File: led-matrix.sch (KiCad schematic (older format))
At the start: 32 parts

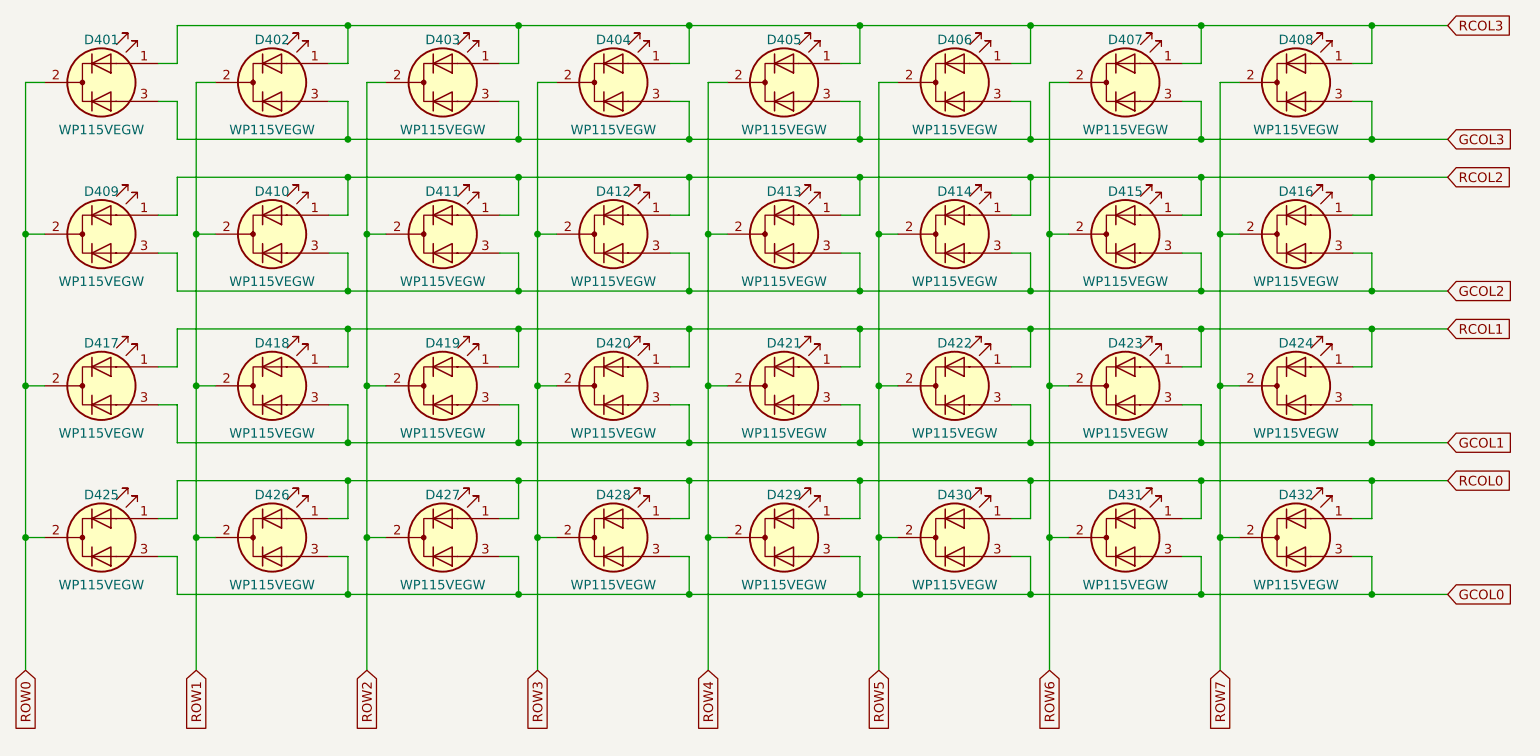
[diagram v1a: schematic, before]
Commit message: renamed led references D -> LED
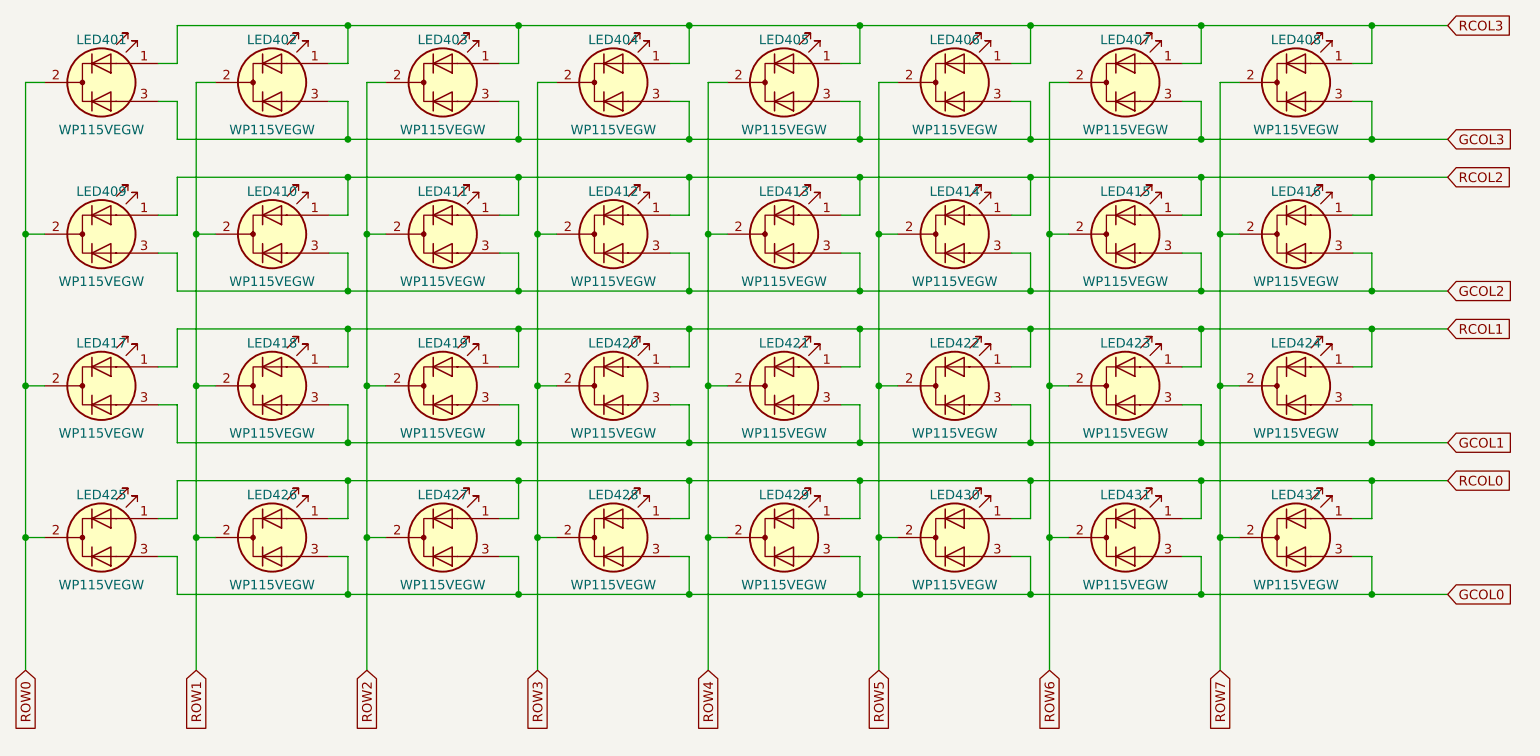
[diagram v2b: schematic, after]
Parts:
- renumbered D401 to LED401, D402 to LED402, D403 to LED403, D404 to LED404, D405 to LED405, D406 to LED406, D407 to LED407, D408 to LED408, D409 to LED409, D410 to LED410, D411 to LED411, D412 to LED412, D413 to LED413, D414 to LED414, D415 to LED415, D416 to LED416, D417 to LED417, D418 to LED418, D419 to LED419, D420 to LED420, D421 to LED421, D422 to LED422, D423 to LED423, D424 to LED424, D425 to LED425, D426 to LED426, D427 to LED427, D428 to LED428, D429 to LED429, D430 to LED430, D431 to LED431, D432 to LED432
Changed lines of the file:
@@
 $EndDescr
 $Comp
-L LED_Dual_ACA D401
+L LED_Dual_ACA LED401
 U 1 1 59DAB354
 P 2400 1900
-F 0 "D401" H 2400 2125 50  0000 C CNN
+F 0 "LED401" H 2400 2125 50  0000 C CNN
 F 1 "WP115VEGW" H 2400 1650 50  0000 C CNN
 F 2 "w_led:WP115VEGW" H 2400 1900 50  0001 C CNN
@@
 $EndComp
 $Comp
-L LED_Dual_ACA D409
+L LED_Dual_ACA LED409
 U 1 1 59DAB3C2
 P 2400 2700
-F 0 "D409" H 2400 2925 50  0000 C CNN
+F 0 "LED409" H 2400 2925 50  0000 C CNN
 F 1 "WP115VEGW" H 2400 2450 50  0000 C CNN
 F 2 "w_led:WP115VEGW" H 2400 2700 50  0001 C CNN
@@
 $EndComp
 $Comp
-L LED_Dual_ACA D417
+L LED_Dual_ACA LED417
 U 1 1 59DAB418
 P 2400 3500
-F 0 "D417" H 2400 3725 50  0000 C CNN
+F 0 "LED417" H 2400 3725 50  0000 C CNN
 F 1 "WP115VEGW" H 2400 3250 50  0000 C CNN
 F 2 "w_led:WP115VEGW" H 2400 3500 50  0001 C CNN
@@
 $EndComp
 $Comp
-L LED_Dual_ACA D425
+L LED_Dual_ACA LED425
 U 1 1 59DAB41E
 P 2400 4300
-F 0 "D425" H 2400 4525 50  0000 C CNN
+F 0 "LED425" H 2400 4525 50  0000 C CNN
 F 1 "WP115VEGW" H 2400 4050 50  0000 C CNN
 F 2 "w_led:WP115VEGW" H 2400 4300 50  0001 C CNN
@@
 $EndComp
 $Comp
-L LED_Dual_ACA D402
+L LED_Dual_ACA LED402
 U 1 1 59DAB4C6
 P 3300 1900
-F 0 "D402" H 3300 2125 50  0000 C CNN
+F 0 "LED402" H 3300 2125 50  0000 C CNN
 F 1 "WP115VEGW" H 3300 1650 50  0000 C CNN
 F 2 "w_led:WP115VEGW" H 3300 1900 50  0001 C CNN
@@
 $EndComp
 $Comp
-L LED_Dual_ACA D410
+L LED_Dual_ACA LED410
 U 1 1 59DAB4CC
 P 3300 2700
-F 0 "D410" H 3300 2925 50  0000 C CNN
+F 0 "LED410" H 3300 2925 50  0000 C CNN
 F 1 "WP115VEGW" H 3300 2450 50  0000 C CNN
 F 2 "w_led:WP115VEGW" H 3300 2700 50  0001 C CNN
@@
 $EndComp
 $Comp
-L LED_Dual_ACA D418
+L LED_Dual_ACA LED418
 U 1 1 59DAB4D2
 P 3300 3500
-F 0 "D418" H 3300 3725 50  0000 C CNN
+F 0 "LED418" H 3300 3725 50  0000 C CNN
 F 1 "WP115VEGW" H 3300 3250 50  0000 C CNN
 F 2 "w_led:WP115VEGW" H 3300 3500 50  0001 C CNN
@@
 $EndComp
 $Comp
-L LED_Dual_ACA D426
+L LED_Dual_ACA LED426
 U 1 1 59DAB4D8
 P 3300 4300
-F 0 "D426" H 3300 4525 50  0000 C CNN
+F 0 "LED426" H 3300 4525 50  0000 C CNN
 F 1 "WP115VEGW" H 3300 4050 50  0000 C CNN
 F 2 "w_led:WP115VEGW" H 3300 4300 50  0001 C CNN
@@
 $EndComp
 $Comp
-L LED_Dual_ACA D403
+L LED_Dual_ACA LED403
 U 1 1 59DAB5EE
 P 4200 1900
-F 0 "D403" H 4200 2125 50  0000 C CNN
+F 0 "LED403" H 4200 2125 50  0000 C CNN
 F 1 "WP115VEGW" H 4200 1650 50  0000 C CNN
 F 2 "w_led:WP115VEGW" H 4200 1900 50  0001 C CNN
@@
 $EndComp
 $Comp
-L LED_Dual_ACA D411
+L LED_Dual_ACA LED411
 U 1 1 59DAB5F4
 P 4200 2700
-F 0 "D411" H 4200 2925 50  0000 C CNN
+F 0 "LED411" H 4200 2925 50  0000 C CNN
 F 1 "WP115VEGW" H 4200 2450 50  0000 C CNN
 F 2 "w_led:WP115VEGW" H 4200 2700 50  0001 C CNN
@@
 $EndComp
 $Comp
-L LED_Dual_ACA D419
+L LED_Dual_ACA LED419
 U 1 1 59DAB5FA
 P 4200 3500
-F 0 "D419" H 4200 3725 50  0000 C CNN
+F 0 "LED419" H 4200 3725 50  0000 C CNN
 F 1 "WP115VEGW" H 4200 3250 50  0000 C CNN
 F 2 "w_led:WP115VEGW" H 4200 3500 50  0001 C CNN
@@
 $EndComp
 $Comp
-L LED_Dual_ACA D427
+L LED_Dual_ACA LED427
 U 1 1 59DAB600
 P 4200 4300
-F 0 "D427" H 4200 4525 50  0000 C CNN
+F 0 "LED427" H 4200 4525 50  0000 C CNN
 F 1 "WP115VEGW" H 4200 4050 50  0000 C CNN
 F 2 "w_led:WP115VEGW" H 4200 4300 50  0001 C CNN
@@
 $EndComp
 $Comp
-L LED_Dual_ACA D404
+L LED_Dual_ACA LED404
 U 1 1 59DAB606
 P 5100 1900
-F 0 "D404" H 5100 2125 50  0000 C CNN
+F 0 "LED404" H 5100 2125 50  0000 C CNN
 F 1 "WP115VEGW" H 5100 1650 50  0000 C CNN
 F 2 "w_led:WP115VEGW" H 5100 1900 50  0001 C CNN
@@
 $EndComp
 $Comp
-L LED_Dual_ACA D412
+L LED_Dual_ACA LED412
 U 1 1 59DAB60C
 P 5100 2700
-F 0 "D412" H 5100 2925 50  0000 C CNN
+F 0 "LED412" H 5100 2925 50  0000 C CNN
 F 1 "WP115VEGW" H 5100 2450 50  0000 C CNN
 F 2 "w_led:WP115VEGW" H 5100 2700 50  0001 C CNN
@@
 $EndComp
 $Comp
-L LED_Dual_ACA D420
+L LED_Dual_ACA LED420
 U 1 1 59DAB612
 P 5100 3500
-F 0 "D420" H 5100 3725 50  0000 C CNN
+F 0 "LED420" H 5100 3725 50  0000 C CNN
 F 1 "WP115VEGW" H 5100 3250 50  0000 C CNN
 F 2 "w_led:WP115VEGW" H 5100 3500 50  0001 C CNN
@@
 $EndComp
 $Comp
-L LED_Dual_ACA D428
+L LED_Dual_ACA LED428
 U 1 1 59DAB618
 P 5100 4300
-F 0 "D428" H 5100 4525 50  0000 C CNN
+F 0 "LED428" H 5100 4525 50  0000 C CNN
 F 1 "WP115VEGW" H 5100 4050 50  0000 C CNN
 F 2 "w_led:WP115VEGW" H 5100 4300 50  0001 C CNN
@@
 $EndComp
 $Comp
-L LED_Dual_ACA D405
+L LED_Dual_ACA LED405
 U 1 1 59DAB7AE
 P 6000 1900
-F 0 "D405" H 6000 2125 50  0000 C CNN
+F 0 "LED405" H 6000 2125 50  0000 C CNN
 F 1 "WP115VEGW" H 6000 1650 50  0000 C CNN
 F 2 "w_led:WP115VEGW" H 6000 1900 50  0001 C CNN
@@
 $EndComp
 $Comp
-L LED_Dual_ACA D413
+L LED_Dual_ACA LED413
 U 1 1 59DAB7B4
 P 6000 2700
-F 0 "D413" H 6000 2925 50  0000 C CNN
+F 0 "LED413" H 6000 2925 50  0000 C CNN
 F 1 "WP115VEGW" H 6000 2450 50  0000 C CNN
 F 2 "w_led:WP115VEGW" H 6000 2700 50  0001 C CNN
@@
 $EndComp
 $Comp
-L LED_Dual_ACA D421
+L LED_Dual_ACA LED421
 U 1 1 59DAB7BA
 P 6000 3500
-F 0 "D421" H 6000 3725 50  0000 C CNN
+F 0 "LED421" H 6000 3725 50  0000 C CNN
 F 1 "WP115VEGW" H 6000 3250 50  0000 C CNN
 F 2 "w_led:WP115VEGW" H 6000 3500 50  0001 C CNN
@@
 $EndComp
 $Comp
-L LED_Dual_ACA D429
+L LED_Dual_ACA LED429
 U 1 1 59DAB7C0
 P 6000 4300
-F 0 "D429" H 6000 4525 50  0000 C CNN
+F 0 "LED429" H 6000 4525 50  0000 C CNN
 F 1 "WP115VEGW" H 6000 4050 50  0000 C CNN
 F 2 "w_led:WP115VEGW" H 6000 4300 50  0001 C CNN
@@
 $EndComp
 $Comp
-L LED_Dual_ACA D406
+L LED_Dual_ACA LED406
 U 1 1 59DAB7C6
 P 6900 1900
-F 0 "D406" H 6900 2125 50  0000 C CNN
+F 0 "LED406" H 6900 2125 50  0000 C CNN
 F 1 "WP115VEGW" H 6900 1650 50  0000 C CNN
 F 2 "w_led:WP115VEGW" H 6900 1900 50  0001 C CNN
@@
 $EndComp
 $Comp
-L LED_Dual_ACA D414
+L LED_Dual_ACA LED414
 U 1 1 59DAB7CC
 P 6900 2700
-F 0 "D414" H 6900 2925 50  0000 C CNN
+F 0 "LED414" H 6900 2925 50  0000 C CNN
 F 1 "WP115VEGW" H 6900 2450 50  0000 C CNN
 F 2 "w_led:WP115VEGW" H 6900 2700 50  0001 C CNN
@@
 $EndComp
 $Comp
-L LED_Dual_ACA D422
+L LED_Dual_ACA LED422
 U 1 1 59DAB7D2
 P 6900 3500
-F 0 "D422" H 6900 3725 50  0000 C CNN
+F 0 "LED422" H 6900 3725 50  0000 C CNN
 F 1 "WP115VEGW" H 6900 3250 50  0000 C CNN
 F 2 "w_led:WP115VEGW" H 6900 3500 50  0001 C CNN
@@
 $EndComp
 $Comp
-L LED_Dual_ACA D430
+L LED_Dual_ACA LED430
 U 1 1 59DAB7D8
 P 6900 4300
-F 0 "D430" H 6900 4525 50  0000 C CNN
+F 0 "LED430" H 6900 4525 50  0000 C CNN
 F 1 "WP115VEGW" H 6900 4050 50  0000 C CNN
 F 2 "w_led:WP115VEGW" H 6900 4300 50  0001 C CNN
@@
 $EndComp
 $Comp
-L LED_Dual_ACA D407
+L LED_Dual_ACA LED407
 U 1 1 59DAB7DE
 P 7800 1900
-F 0 "D407" H 7800 2125 50  0000 C CNN
+F 0 "LED407" H 7800 2125 50  0000 C CNN
 F 1 "WP115VEGW" H 7800 1650 50  0000 C CNN
 F 2 "w_led:WP115VEGW" H 7800 1900 50  0001 C CNN
@@
 $EndComp
 $Comp
-L LED_Dual_ACA D415
+L LED_Dual_ACA LED415
 U 1 1 59DAB7E4
 P 7800 2700
-F 0 "D415" H 7800 2925 50  0000 C CNN
+F 0 "LED415" H 7800 2925 50  0000 C CNN
 F 1 "WP115VEGW" H 7800 2450 50  0000 C CNN
 F 2 "w_led:WP115VEGW" H 7800 2700 50  0001 C CNN
@@
 $EndComp
 $Comp
-L LED_Dual_ACA D423
+L LED_Dual_ACA LED423
 U 1 1 59DAB7EA
 P 7800 3500
-F 0 "D423" H 7800 3725 50  0000 C CNN
+F 0 "LED423" H 7800 3725 50  0000 C CNN
 F 1 "WP115VEGW" H 7800 3250 50  0000 C CNN
 F 2 "w_led:WP115VEGW" H 7800 3500 50  0001 C CNN
@@
 $EndComp
 $Comp
-L LED_Dual_ACA D431
+L LED_Dual_ACA LED431
 U 1 1 59DAB7F0
 P 7800 4300
-F 0 "D431" H 7800 4525 50  0000 C CNN
+F 0 "LED431" H 7800 4525 50  0000 C CNN
 F 1 "WP115VEGW" H 7800 4050 50  0000 C CNN
 F 2 "w_led:WP115VEGW" H 7800 4300 50  0001 C CNN
@@
 $EndComp
 $Comp
-L LED_Dual_ACA D408
+L LED_Dual_ACA LED408
 U 1 1 59DAB7F6
 P 8700 1900
-F 0 "D408" H 8700 2125 50  0000 C CNN
+F 0 "LED408" H 8700 2125 50  0000 C CNN
 F 1 "WP115VEGW" H 8700 1650 50  0000 C CNN
 F 2 "w_led:WP115VEGW" H 8700 1900 50  0001 C CNN
@@
 $EndComp
 $Comp
-L LED_Dual_ACA D416
+L LED_Dual_ACA LED416
 U 1 1 59DAB7FC
 P 8700 2700
-F 0 "D416" H 8700 2925 50  0000 C CNN
+F 0 "LED416" H 8700 2925 50  0000 C CNN
 F 1 "WP115VEGW" H 8700 2450 50  0000 C CNN
 F 2 "w_led:WP115VEGW" H 8700 2700 50  0001 C CNN
@@
 $EndComp
 $Comp
-L LED_Dual_ACA D424
+L LED_Dual_ACA LED424
 U 1 1 59DAB802
 P 8700 3500
-F 0 "D424" H 8700 3725 50  0000 C CNN
+F 0 "LED424" H 8700 3725 50  0000 C CNN
 F 1 "WP115VEGW" H 8700 3250 50  0000 C CNN
 F 2 "w_led:WP115VEGW" H 8700 3500 50  0001 C CNN
@@
 $EndComp
 $Comp
-L LED_Dual_ACA D432
+L LED_Dual_ACA LED432
 U 1 1 59DAB808
 P 8700 4300
-F 0 "D432" H 8700 4525 50  0000 C CNN
+F 0 "LED432" H 8700 4525 50  0000 C CNN
 F 1 "WP115VEGW" H 8700 4050 50  0000 C CNN
 F 2 "w_led:WP115VEGW" H 8700 4300 50  0001 C CNN

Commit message: work in progress
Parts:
- LED401, LED402, LED403, LED404, LED405, LED406, LED407, LED408, LED409, LED410, LED411, LED412, LED413, LED414, LED415, LED416, LED417, LED418, LED419, LED420, LED421, LED422, LED423, LED424, LED425, LED426, LED427, LED428, LED429, LED430, LED431, LED432: footprint w_led:WP115VEGW -> w_led:LTL1BEKVJNN

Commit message: cleanup
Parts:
- LED401, LED402, LED403, LED404, LED405, LED406, LED407, LED408, LED409, LED410, LED411, LED412, LED413, LED414, LED415, LED416, LED417, LED418, LED419, LED420, LED421, LED422, LED423, LED424, LED425, LED426, LED427, LED428, LED429, LED430, LED431, LED432: value WP115VEGW -> LTL1BEKVJNN; MFN Kingbright -> Lite-On; MFP WP115VEGW -> LTL1BEKVJNN
